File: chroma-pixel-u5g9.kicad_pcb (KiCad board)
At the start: 2 copper layers, 76 x 78 mm, 106 parts, among them J1 Conn_ST_STDC14, J2 LCD_ST7701s, J3 USB_C_Receptacle_USB2.0_16P, J4 USB_C_Receptacle_USB2.0_16P, SW1 SW_Push, SW2 SW_Push, SW3 SW_SPDT, U1 STM32U5G9ZJTxQ, U2 MX66LM1G45GXDI00, U3 TPS61042DRBT, U4 USBLC6-2SC6, U5 BQ24075RGT, U6 BQ27441DRZR-G1A, U7 TPS61023DRLT, Y1 16MHz, Y2 32.768KHz

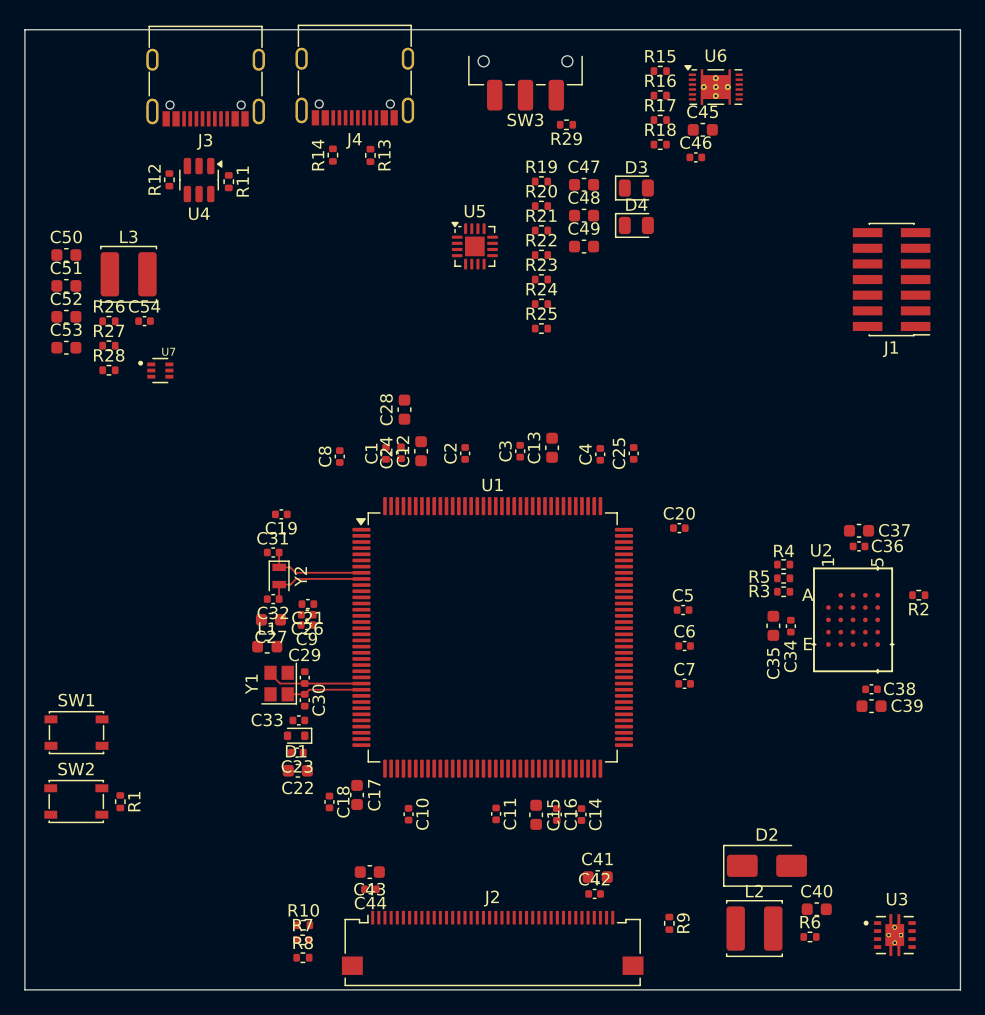
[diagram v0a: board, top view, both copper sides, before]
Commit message: Add connection from OSPI Flash and LCD to MCU
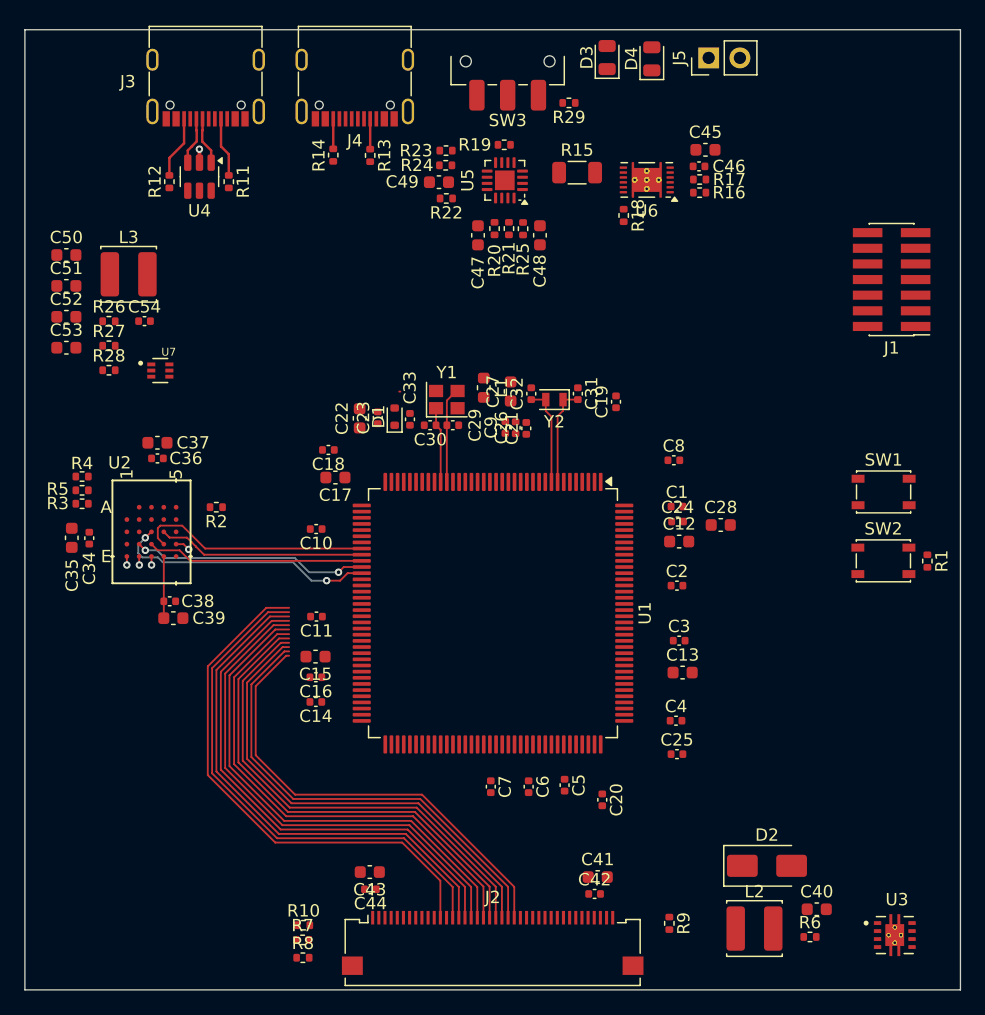
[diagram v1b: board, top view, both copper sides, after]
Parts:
- added J5: Conn_01x02, Connector_PinHeader_2.54mm:PinHeader_1x02_P2.54mm_Vertical, F.Cu at (145.4, 57.7)
- R15: footprint Resistor_SMD:R_0402_1005Metric -> Resistor_SMD:R_1206_3216Metric
- moved SW1 68.4 mm to (159.6, 93.0)
- moved SW2 68.4 mm to (159.6, 98.6)
- moved R1 68.4 mm to (163.1, 98.6)
- moved R2 57.5 mm to (105.4, 94.2)
- moved C38 57.5 mm to (101.6, 101.9)
- moved C35 57.4 mm to (93.6, 96.7)
- moved C36 57.4 mm to (100.6, 90.3)
- moved C37 57.4 mm to (100.6, 89.0)
- moved R3 57.4 mm to (94.5, 94.0)
- moved R4 57.4 mm to (94.5, 91.7)
- moved R5 57.4 mm to (94.5, 92.9)
- moved C34 57.4 mm to (95.0, 96.7)
- moved U2 57.4 mm to (100.1, 96.2)
- moved C39 57.2 mm to (101.9, 103.3)
- moved C22 29.1 mm to (117.0, 87.0), turned to 90 degrees
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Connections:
- R3 pad 1: /OCTOSPI/~{CS} -> /MCU/~{OSPI_CS}
- R4 pad 2: /OCTOSPI/SCLK -> /MCU/OSPI_SCLK
- U1 pad 116: unconnected-(U1-PD0-Pad116) -> /DISPLAY/LCD_B4
- U1 pad 117: unconnected-(U1-PD1-Pad117) -> /DISPLAY/LCD_B5
- U1 pad 119: unconnected-(U1-PD3-Pad119) -> /DISPLAY/LCD_PCLK
- U1 pad 123: unconnected-(U1-PD6-Pad123) -> /DISPLAY/LCD_DE
- U1 pad 141: unconnected-(U1-PE0-Pad141) -> /DISPLAY/LCD_HSYNC
- U1 pad 29: unconnected-(U1-PC0-Pad29) -> /MCU/SIO7
- U1 pad 30: unconnected-(U1-PC1-Pad30) -> /MCU/SIO4
- U1 pad 31: unconnected-(U1-PC2-Pad31) -> /MCU/SIO5
- U1 pad 32: unconnected-(U1-PC3-Pad32) -> /MCU/SIO6
- U1 pad 38: unconnected-(U1-PA2-Pad38) -> /MCU/~{OSPI_CS}
- U1 pad 39: unconnected-(U1-PA3-Pad39) -> /MCU/OSPI_SCLK
- U1 pad 44: unconnected-(U1-PA6-Pad44) -> /MCU/SIO3
- U1 pad 45: unconnected-(U1-PA7-Pad45) -> /MCU/SIO2
- U1 pad 46: unconnected-(U1-PB0-Pad46) -> /MCU/SIO0
- U1 pad 47: unconnected-(U1-PB1-Pad47) -> /MCU/SIO1
- U1 pad 48: unconnected-(U1-PB2-Pad48) -> /OCTOSPI/DQS
- U1 pad 51: unconnected-(U1-PE7-Pad51) -> /DISPLAY/LCD_B6
- U1 pad 52: unconnected-(U1-PE8-Pad52) -> /DISPLAY/LCD_B7
- U1 pad 53: unconnected-(U1-PE9-Pad53) -> /DISPLAY/LCD_G2
- U1 pad 56: unconnected-(U1-PE10-Pad56) -> /DISPLAY/LCD_G3
- U1 pad 57: unconnected-(U1-PE11-Pad57) -> /DISPLAY/LCD_G4
- U1 pad 58: unconnected-(U1-PE12-Pad58) -> /DISPLAY/LCD_G5
- U1 pad 59: unconnected-(U1-PE13-Pad59) -> /DISPLAY/LCD_G6
- U1 pad 60: unconnected-(U1-PE14-Pad60) -> /DISPLAY/LCD_G7
- U1 pad 73: unconnected-(U1-PD8-Pad73) -> /DISPLAY/LCD_R3
- U1 pad 74: unconnected-(U1-PD9-Pad74) -> /DISPLAY/LCD_R4
- U1 pad 75: unconnected-(U1-PD10-Pad75) -> /DISPLAY/LCD_R5
- U1 pad 76: unconnected-(U1-PD11-Pad76) -> /DISPLAY/LCD_R6
- U1 pad 77: unconnected-(U1-PD12-Pad77) -> /DISPLAY/LCD_R7
- U1 pad 78: unconnected-(U1-PD13-Pad78) -> /DISPLAY/LCD_VSYNC
- U1 pad 79: unconnected-(U1-PD14-Pad79) -> /DISPLAY/LCD_B3
- U2 pad C4: /OCTOSPI/SIO2 -> /MCU/SIO2
- U2 pad D2: /OCTOSPI/SIO1 -> /MCU/SIO1
- U2 pad D3: /OCTOSPI/SIO0 -> /MCU/SIO0
- U2 pad D4: /OCTOSPI/SIO3 -> /MCU/SIO3
- U2 pad D5: /OCTOSPI/SIO4 -> /MCU/SIO4
- U2 pad E1: /OCTOSPI/SIO7 -> /MCU/SIO7
- U2 pad E2: /OCTOSPI/SIO6 -> /MCU/SIO6
- U2 pad E3: /OCTOSPI/SIO5 -> /MCU/SIO5
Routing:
- net /DISPLAY/LCD_B3: track 0.00 -> 42.9 mm
- net /DISPLAY/LCD_G7: track 0.00 -> 42.6 mm
- net /DISPLAY/LCD_G6: track 0.00 -> 42.0 mm
- net /DISPLAY/LCD_G5: track 0.00 -> 41.5 mm
- net /DISPLAY/LCD_G4: track 0.00 -> 41.0 mm
- net /DISPLAY/LCD_G3: track 0.00 -> 40.5 mm
- net /DISPLAY/LCD_G2: track 0.00 -> 39.9 mm
- net /DISPLAY/LCD_R7: track 0.00 -> 39.4 mm
- net /DISPLAY/LCD_R6: track 0.00 -> 38.8 mm
- net /DISPLAY/LCD_R5: track 0.00 -> 38.3 mm
- net /DISPLAY/LCD_R4: track 0.00 -> 37.8 mm
- net /DISPLAY/LCD_R3: track 0.00 -> 37.3 mm
- net /OCTOSPI/DQS: track 0.00 -> 21.5 mm, vias 0 -> 2
- net /MCU/SIO1: track 0.00 -> 19.2 mm, vias 0 -> 2
- net /MCU/SIO3: track 0.00 -> 18.9 mm
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
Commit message: Change bypass capacitor to 0201
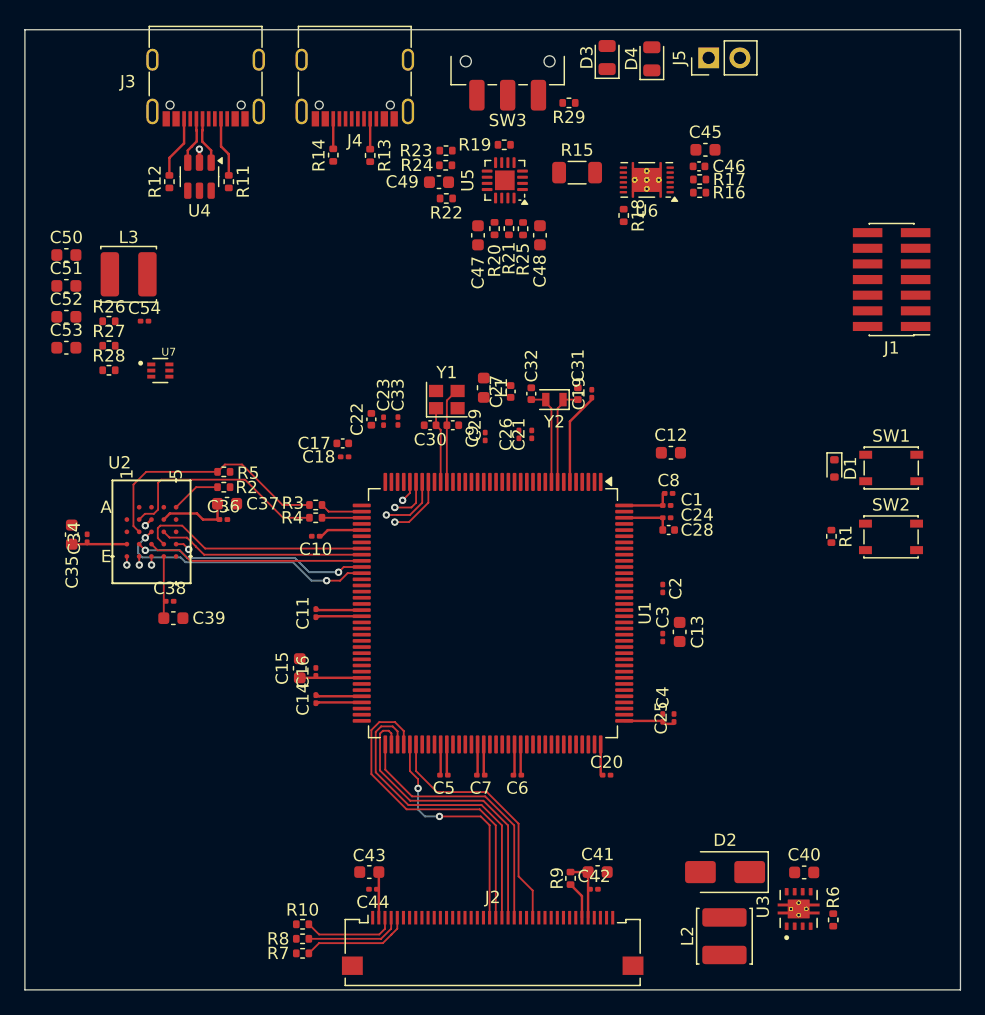
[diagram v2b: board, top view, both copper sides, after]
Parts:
- C1, C10, C11, C14, C16, C18, C19, C2, C20, C21, C23, C24, C25, C26, C3, C33, C34, C36, C38, C4, C42, C44, C5, C54, C6, C7, C8, C9: footprint Capacitor_SMD:C_0402_1005Metric -> Capacitor_SMD:C_0201_0603Metric
- C17, C22, C27, C28: footprint Capacitor_SMD:C_0603_1608Metric -> Capacitor_SMD:C_0402_1005Metric
- moved D1 36.0 mm to (155.6, 91.1), turned to -90 degrees
- moved R4 19.3 mm to (113.4, 95.1), turned to 0 degrees
- moved R3 19.0 mm to (113.4, 94.1), turned to 180 degrees
- moved R5 11.6 mm to (106.0, 91.4), turned to 180 degrees
- moved C5 9.84 mm to (123.9, 116.0), turned to 180 degrees
- moved R9 8.82 mm to (134.1, 124.4)
- moved U3 8.09 mm to (152.7, 126.9), turned to 90 degrees
- moved R1 8.05 mm to (155.3, 96.6)
- moved C37 7.52 mm to (106.2, 94.0), turned to 0 degrees
- moved C36 7.31 mm to (105.9, 95.2), turned to 0 degrees
- moved C12 7.24 mm to (142.3, 89.8)
- moved C28 4.25 mm to (142.1, 96.1)
- moved D2 3.44 mm to (146.7, 123.9), turned to 180 degrees
- moved C13 3.31 mm to (143.0, 104.4), turned to 90 degrees
- moved C40 3.16 mm to (153.1, 123.9)
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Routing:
- net /DISPLAY/LCD_B3: track 42.9 -> 0.00 mm
- net /DISPLAY/LCD_G7: track 42.6 -> 0.00 mm
- net /DISPLAY/LCD_G6: track 42.0 -> 0.00 mm
- net /DISPLAY/LCD_G5: track 41.5 -> 0.00 mm
- net /DISPLAY/LCD_G4: track 41.0 -> 0.00 mm
- net /DISPLAY/LCD_G3: track 40.5 -> 0.00 mm
- net /DISPLAY/LCD_G2: track 39.9 -> 0.00 mm
- net VDD_MCU: track 0.00 -> 26.9 mm
- net /DISPLAY/LCD_VSYNC: track 0.00 -> 20.4 mm
- net Net-(U2-~{CS}): track 0.00 -> 20.4 mm
- net /DISPLAY/LCD_R7: track 39.4 -> 19.4 mm, vias 0 -> 2
- net +3V3: track 5.01 -> 24.4 mm
- net Net-(U2-SCLK): track 0.00 -> 17.7 mm
- net GND: track 1.10 -> 17.0 mm, vias 1 -> 2
- net /DISPLAY/LCD_R3: track 37.3 -> 21.9 mm
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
